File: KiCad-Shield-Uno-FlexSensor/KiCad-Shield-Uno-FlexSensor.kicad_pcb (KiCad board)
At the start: 2 copper layers, 68.6 x 53.3 mm, 8 parts, among them J1 Power, J2 Digital/PWM, J3 Analog, J4 Digital/PWM

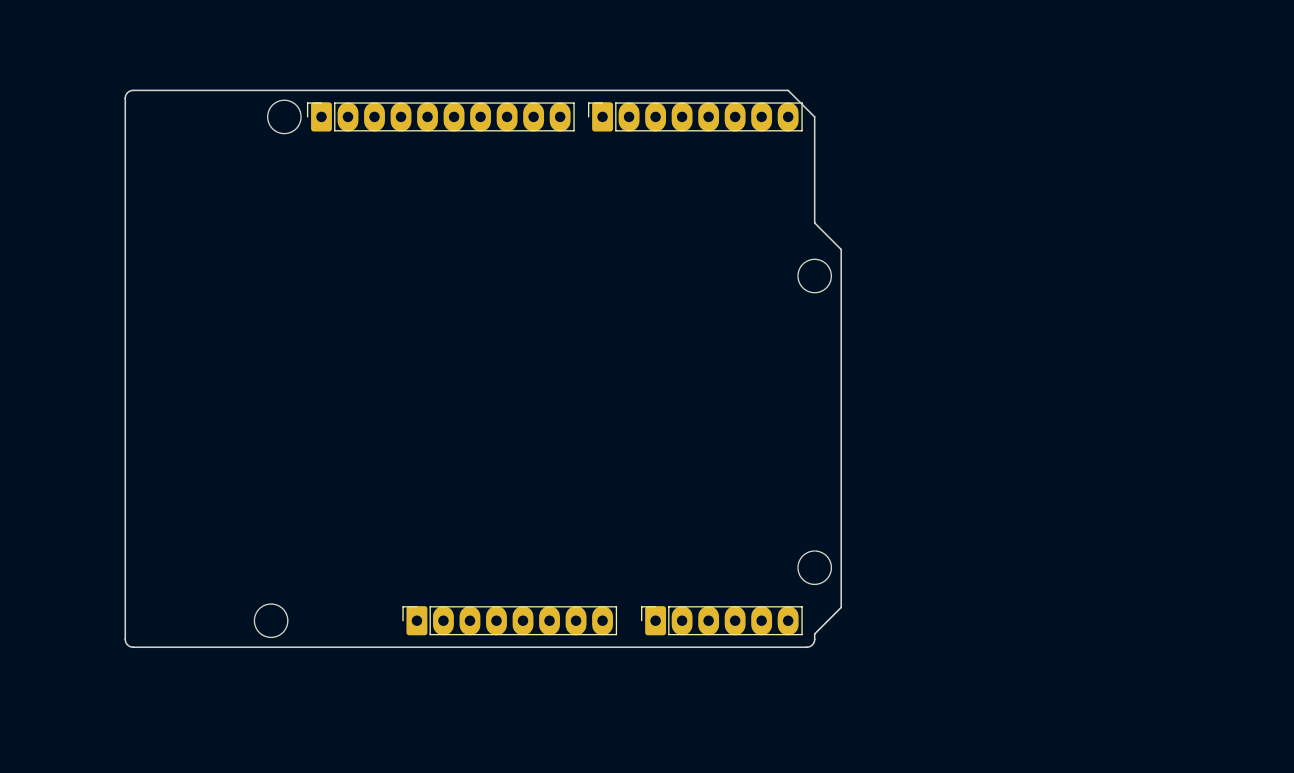
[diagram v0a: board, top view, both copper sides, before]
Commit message: Ajout des contraintes du design manager pour le routage à l'INSA
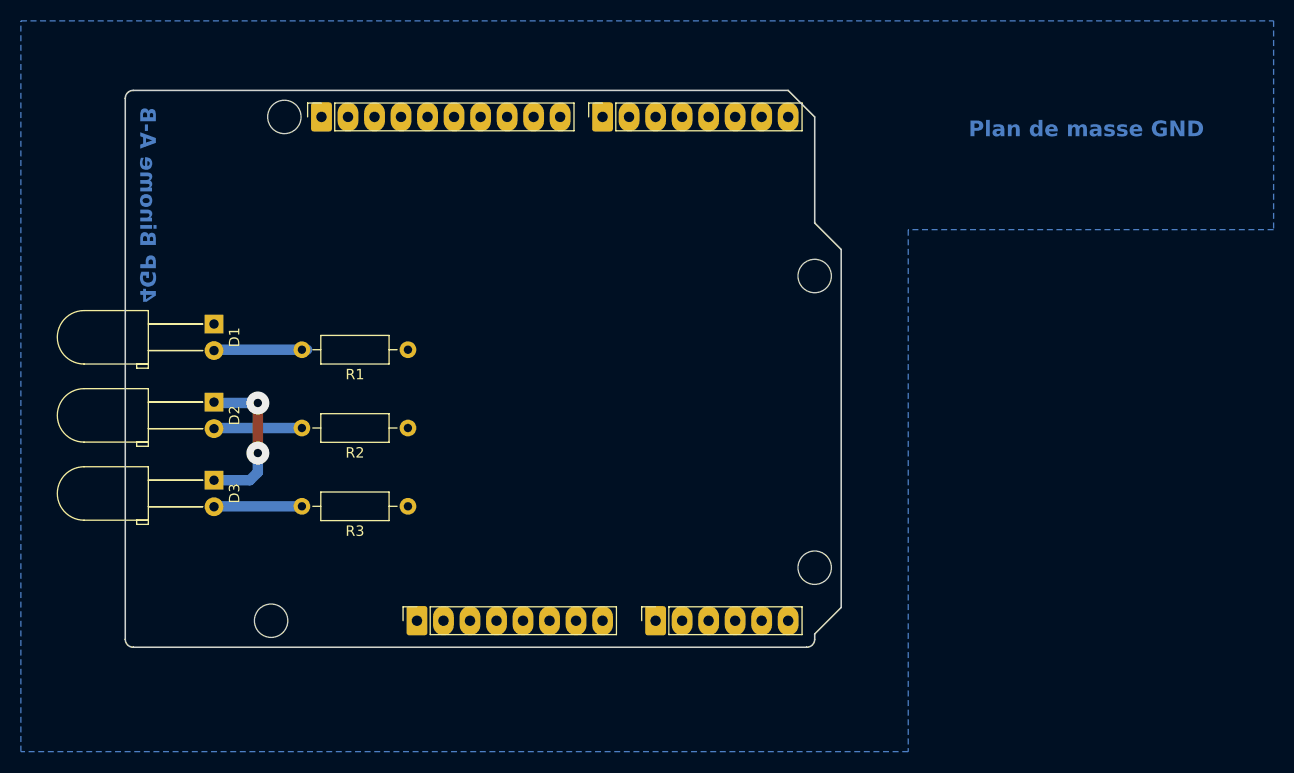
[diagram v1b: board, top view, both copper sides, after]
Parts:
- added D1: STAT, LED_THT:LED_D5.0mm_Horizontal_O6.35mm_Z3.0mm, F.Cu at (108.5, 69.0)
- added D2: MODE, LED_THT:LED_D5.0mm_Horizontal_O6.35mm_Z3.0mm, F.Cu at (108.5, 76.5)
- added D3: ERR, LED_THT:LED_D5.0mm_Horizontal_O6.35mm_Z3.0mm, F.Cu at (108.5, 84.0)
- added R1: 680, Resistor_THT:R_Axial_DIN0207_L6.3mm_D2.5mm_P10.16mm_Horizontal, F.Cu at (127.1, 71.5)
- added R2: 680, Resistor_THT:R_Axial_DIN0207_L6.3mm_D2.5mm_P10.16mm_Horizontal, F.Cu at (127.1, 79.0)
- added R3: 680, Resistor_THT:R_Axial_DIN0207_L6.3mm_D2.5mm_P10.16mm_Horizontal, F.Cu at (127.1, 86.5)
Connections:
- J2 pad 10: unconnected-(J2-Pin_10-Pad10) -> /D8
- J2 pad 7: unconnected-(J2-Pin_7-Pad7) -> /D11
- J2 pad 8: unconnected-(J2-Pin_8-Pad8) -> /D10
- J2 pad 9: unconnected-(J2-Pin_9-Pad9) -> /D9
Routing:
- net GND: track 0.00 -> 15.4 mm, vias 0 -> 2
- net Net-(D1-A): track 0.00 -> 8.95 mm
- net Net-(D2-A): track 0.00 -> 8.44 mm
- net Net-(D3-A): track 0.00 -> 8.44 mm
- added copper zone on B.Cu, net GND
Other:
- board text added: "4GP Binome A-B"
- board text added: "Plan de masse GND"
